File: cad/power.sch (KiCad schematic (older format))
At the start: 29 parts, among them SW1 SW_PUSH_4, U3 TPS73001, U4 TPS73001

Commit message: everything has a footprint
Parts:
- BT1: footprint (none) -> Pin_Headers:Pin_Header_Straight_1x02
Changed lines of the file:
@@
 F 0 "BT1" H 6850 6350 50  0000 C CNN
 F 1 "BATTERY" H 6850 5960 50  0000 C CNN
-F 2 "" H 6850 6150 60  0001 C CNN
+F 2 "Pin_Headers:Pin_Header_Straight_1x02" H 6850 6150 60  0001 C CNN
 F 3 "" H 6850 6150 60  0000 C CNN
 	1    6850 6150

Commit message: progress check in
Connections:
- net EN: no longer U3.3 (EN), U4.3 (EN)
- net EN_REG: now reaches C19.1, D3.3, R10.1
- net EN_REG: now also U3.3 (EN), U4.3 (EN)
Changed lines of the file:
@@
 	4750 2500 4400 2500
 Text Label 4400 2500 0    60   ~ 0
-EN
+EN_REG
 $Comp
 L C C21
@@
 	4750 4050 4400 4050
 Text Label 4400 4050 0    60   ~ 0
-EN
+EN_REG
 $Comp
 L AGND #PWR047
@@
 	2850 6150 2850 6250
 Wire Wire Line
-	2850 6150 3150 6150
+	2850 6150 3500 6150
 Wire Wire Line
 	3150 6150 3150 6250
@@
 	1450 6250 1450 6300
 Connection ~ 1450 6250
+Connection ~ 2850 6150
+Connection ~ 3150 6150
+Text Label 3300 6150 0    60   ~ 0
+EN_REG
 $EndSCHEMATC

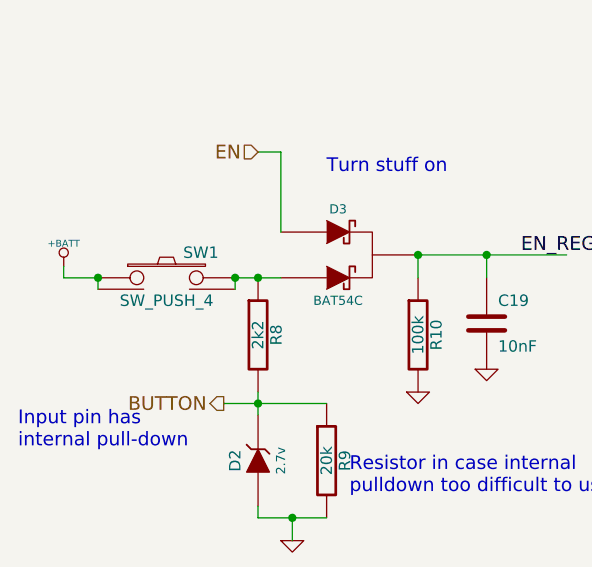
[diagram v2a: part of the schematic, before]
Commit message: components placed again
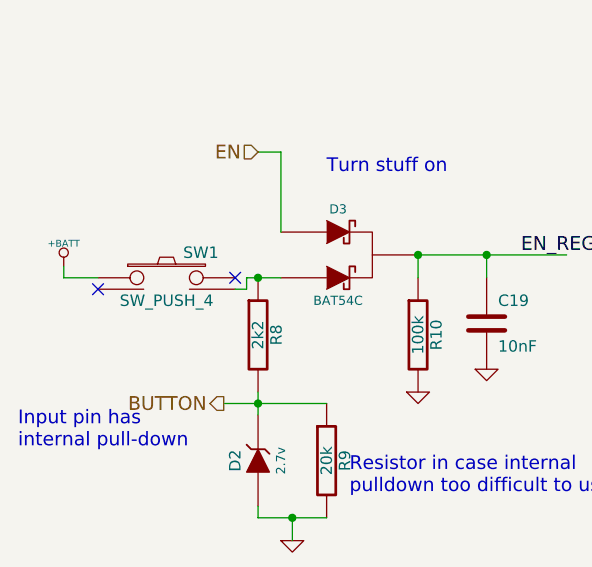
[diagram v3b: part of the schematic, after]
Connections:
- net +BATT: no longer SW1.2
- net at D3.2, R8.1, SW1.4: no longer SW1.3
- no-connect marks 0 -> 2
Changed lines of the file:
@@
 	1    0    0    -1
 $EndComp
-Wire Wire Line
-	3950 2250 3950 2400
-Connection ~ 3950 2400
 $Comp
 L C C22
@@
 	1    0    0    -1
 $EndComp
-Wire Wire Line
-	3950 2400 4750 2400
-Wire Wire Line
-	4750 2600 4700 2600
-Wire Wire Line
-	4700 2600 4700 3100
 $Comp
 L GND #PWR038
@@
 	0    1    1    0
 $EndComp
-Wire Wire Line
-	5800 3200 5900 3200
-Wire Wire Line
-	5900 3200 5900 3300
-Wire Wire Line
-	5300 3200 5200 3200
-Wire Wire Line
-	5200 3200 5200 3300
 $Comp
 L R R16
@@
 	1    0    0    -1
 $EndComp
-Wire Wire Line
-	5750 2400 7350 2400
 $Comp
 L VCC #PWR041
@@
 	1    0    0    -1
 $EndComp
-Wire Wire Line
-	6500 2400 6500 2450
-Connection ~ 6500 2400
-Connection ~ 6200 2400
-Wire Wire Line
-	5750 2600 6000 2600
-Wire Wire Line
-	6000 2600 6000 2950
-Wire Wire Line
-	6000 2950 6200 2950
-Wire Wire Line
-	6200 2900 6200 3000
-Connection ~ 6200 2950
-Wire Wire Line
-	6500 2850 6500 2900
-Wire Wire Line
-	6500 2900 6200 2900
-Connection ~ 6200 2900
 $Comp
 L DGND #PWR042
@@
 	1    0    0    -1
 $EndComp
-Connection ~ 7000 2400
-Wire Wire Line
-	4750 2500 4400 2500
 Text Label 4400 2500 0    60   ~ 0
 EN_REG
@@
 	1    0    0    -1
 $EndComp
-Wire Wire Line
-	4750 4150 4700 4150
-Wire Wire Line
-	4700 4150 4700 4650
 $Comp
 L GND #PWR045
@@
 	0    1    1    0
 $EndComp
-Wire Wire Line
-	5800 4750 5900 4750
-Wire Wire Line
-	5900 4750 5900 4850
-Wire Wire Line
-	5300 4750 5200 4750
-Wire Wire Line
-	5200 4750 5200 4850
 $Comp
 L R R18
@@
 	1    0    0    -1
 $EndComp
-Wire Wire Line
-	5750 3950 7350 3950
-Wire Wire Line
-	6500 3950 6500 4000
-Connection ~ 6500 3950
-Connection ~ 6200 3950
-Wire Wire Line
-	5750 4150 6000 4150
-Wire Wire Line
-	6000 4150 6000 4500
-Wire Wire Line
-	6000 4500 6200 4500
-Wire Wire Line
-	6200 4450 6200 4550
-Connection ~ 6200 4500
-Wire Wire Line
-	6500 4400 6500 4450
-Wire Wire Line
-	6500 4450 6200 4450
-Connection ~ 6200 4450
-Connection ~ 7000 3950
-Wire Wire Line
-	4750 4050 4400 4050
 Text Label 4400 4050 0    60   ~ 0
 EN_REG
@@
 	1    0    0    -1
 $EndComp
-Wire Wire Line
-	2500 3950 3300 3950
-Connection ~ 3150 3950
-Connection ~ 2800 3950
-Wire Wire Line
-	3800 3950 4750 3950
-Connection ~ 3950 3950
 $Comp
 L GND #PWR052
@@
 	1    0    0    -1
 $EndComp
-Wire Wire Line
-	1300 6200 1300 6250
-Wire Wire Line
-	1300 6250 1450 6250
 Text HLabel 2150 5700 0    60   Input ~ 0
 EN
-Wire Wire Line
-	2150 5700 2250 5700
 $Comp
 L R R10
@@
 	1    0    0    -1
 $EndComp
-Wire Wire Line
-	2150 6750 2150 6850
-Wire Wire Line
-	2000 6800 2450 6800
-Connection ~ 2150 6800
 $Comp
 L C C19
@@
 	1    0    0    -1
 $EndComp
-Wire Wire Line
-	2050 6250 2250 6250
-Connection ~ 2150 6250
 Text Notes 1100 7000 0    60   ~ 0
 Input pin has\ninternal pull-down
@@
 	1    0    0    -1
 $EndComp
-Wire Wire Line
-	2150 7250 2150 7300
-Wire Wire Line
-	2150 7300 2450 7300
 $Comp
 L GND #PWR058
@@
 	1    0    0    -1
 $EndComp
-Wire Wire Line
-	2300 7400 2300 7300
-Connection ~ 2300 7300
 Text Notes 2550 7200 0    60   ~ 0
 Resistor in case internal\npulldown too difficult to use
@@
 	1    0    0    -1
 $EndComp
-Wire Wire Line
-	5300 6500 5300 6600
-Wire Wire Line
-	5300 5950 5300 6000
 $Comp
 L GND #PWR060
@@
 Text HLabel 4900 6550 0    60   Output ~ 0
 BATTVOLT
-Wire Wire Line
-	4900 6550 5300 6550
-Connection ~ 5300 6550
 $Comp
 L DGND #PWR061
@@
 	-1   0    0    1
 $EndComp
-Wire Wire Line
-	9650 6050 9650 6200
-Wire Wire Line
-	9100 6150 9100 6250
-Wire Wire Line
-	8800 6250 8800 6150
-Wire Wire Line
-	8450 6150 8450 6250
 $Comp
 L PWR_FLAG #FLG069
@@
 	1    0    0    -1
 $EndComp
-Connection ~ 4200 3950
 $Comp
 L BAT54C D3
@@
 	1    0    0    -1
 $EndComp
-Wire Wire Line
-	2250 5700 2250 6050
-Wire Wire Line
-	2850 6150 2850 6250
-Wire Wire Line
-	2850 6150 3500 6150
-Wire Wire Line
-	3150 6150 3150 6250
 $Comp
 L TPS73001 U3
@@
 	1    0    0    -1
 $EndComp
-Wire Wire Line
-	2050 6300 2050 6250
-Connection ~ 2050 6250
-Wire Wire Line
-	1450 6250 1450 6300
-Connection ~ 1450 6250
+Text Label 3300 6150 0    60   ~ 0
+EN_REG
+Wire Wire Line
+	3950 2250 3950 2400
+Connection ~ 3950 2400
+Wire Wire Line
+	3950 2400 4750 2400
+Wire Wire Line
+	4750 2600 4700 2600
+Wire Wire Line
+	4700 2600 4700 3100
+Wire Wire Line
+	5800 3200 5900 3200
+Wire Wire Line
+	5900 3200 5900 3300
+Wire Wire Line
+	5300 3200 5200 3200
+Wire Wire Line
+	5200 3200 5200 3300
+Wire Wire Line
+	5750 2400 7350 2400
+Wire Wire Line
+	6500 2400 6500 2450
+Connection ~ 6500 2400
+Connection ~ 6200 2400
+Wire Wire Line
+	5750 2600 6000 2600
+Wire Wire Line
+	6000 2600 6000 2950
+Wire Wire Line
+	6000 2950 6200 2950
+Wire Wire Line
+	6200 2900 6200 3000
+Connection ~ 6200 2950
+Wire Wire Line
+	6500 2850 6500 2900
+Wire Wire Line
+	6500 2900 6200 2900
+Connection ~ 6200 2900
+Connection ~ 7000 2400
+Wire Wire Line
+	4750 2500 4400 2500
+Wire Wire Line
+	4750 4150 4700 4150
+Wire Wire Line
+	4700 4150 4700 4650
+Wire Wire Line
+	5800 4750 5900 4750
+Wire Wire Line
+	5900 4750 5900 4850
+Wire Wire Line
+	5300 4750 5200 4750
+Wire Wire Line
+	5200 4750 5200 4850
+Wire Wire Line
+	5750 3950 7350 3950
+Wire Wire Line
+	6500 3950 6500 4000
+Connection ~ 6500 3950
+Connection ~ 6200 3950
+Wire Wire Line
+	5750 4150 6000 4150
+Wire Wire Line
+	6000 4150 6000 4500
+Wire Wire Line
+	6000 4500 6200 4500
+Wire Wire Line
+	6200 4450 6200 4550
+Connection ~ 6200 4500
+Wire Wire Line
+	6500 4400 6500 4450
+Wire Wire Line
+	6500 4450 6200 4450
+Connection ~ 6200 4450
+Connection ~ 7000 3950
+Wire Wire Line
+	4750 4050 4400 4050
+Wire Wire Line
+	2500 3950 3300 3950
+Connection ~ 3150 3950
+Connection ~ 2800 3950
+Wire Wire Line
+	3800 3950 4750 3950
+Connection ~ 3950 3950
+Wire Wire Line
+	1300 6200 1300 6250
+Wire Wire Line
+	2150 5700 2250 5700
+Wire Wire Line
+	2150 6750 2150 6850
+Wire Wire Line
+	2000 6800 2450 6800
+Connection ~ 2150 6800
+Wire Wire Line
+	2150 7250 2150 7300
+Wire Wire Line
+	2150 7300 2450 7300
+Wire Wire Line
+	2300 7400 2300 7300
+Connection ~ 2300 7300
+Wire Wire Line
+	5300 6500 5300 6600
+Wire Wire Line
+	5300 5950 5300 6000
+Wire Wire Line
+	4900 6550 5300 6550
+Connection ~ 5300 6550
+Wire Wire Line
+	9650 6050 9650 6200
+Wire Wire Line
+	9100 6150 9100 6250
+Wire Wire Line
+	8800 6250 8800 6150
+Wire Wire Line
+	8450 6150 8450 6250
+Connection ~ 4200 3950
+Wire Wire Line
+	2250 5700 2250 6050
+Wire Wire Line
+	2850 6150 2850 6250
+Wire Wire Line
+	2850 6150 3500 6150
+Wire Wire Line
+	3150 6150 3150 6250
 Connection ~ 2850 6150
 Connection ~ 3150 6150
-Text Label 3300 6150 0    60   ~ 0
-EN_REG
+Wire Wire Line
+	1300 6250 1450 6250
+Wire Wire Line
+	2050 6300 2100 6300
+Wire Wire Line
+	2100 6300 2100 6250
+Wire Wire Line
+	2100 6250 2250 6250
+Connection ~ 2150 6250
+NoConn ~ 2050 6250
+NoConn ~ 1450 6300
 $EndSCHEMATC
